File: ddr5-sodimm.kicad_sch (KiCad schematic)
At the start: 1 part, among them J4001 BUS_DDR5_SODIMM_AMPHENOL_1016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

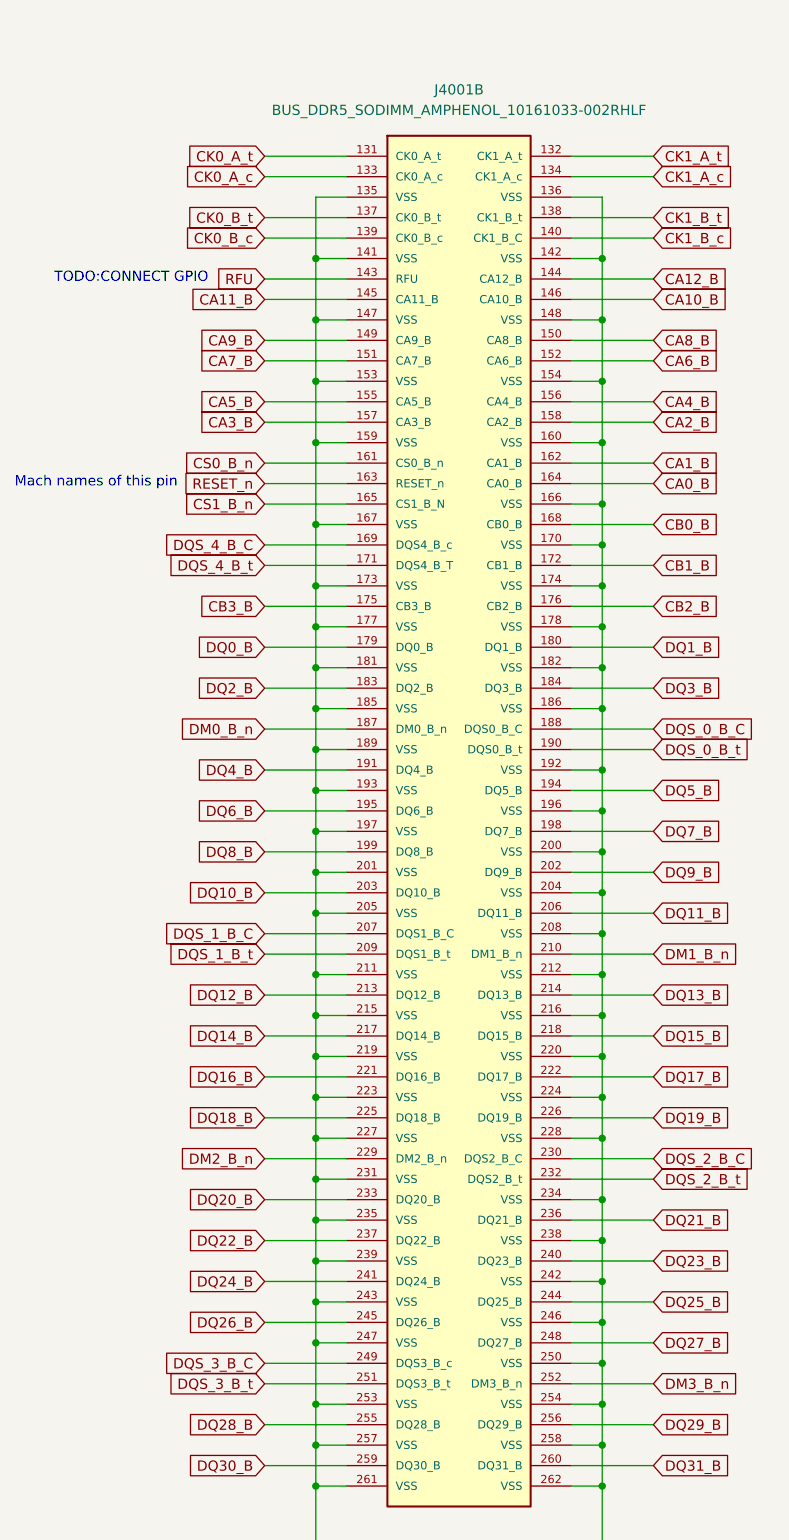
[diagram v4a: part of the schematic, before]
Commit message: Create pinout and fanout for FPGA bank 34
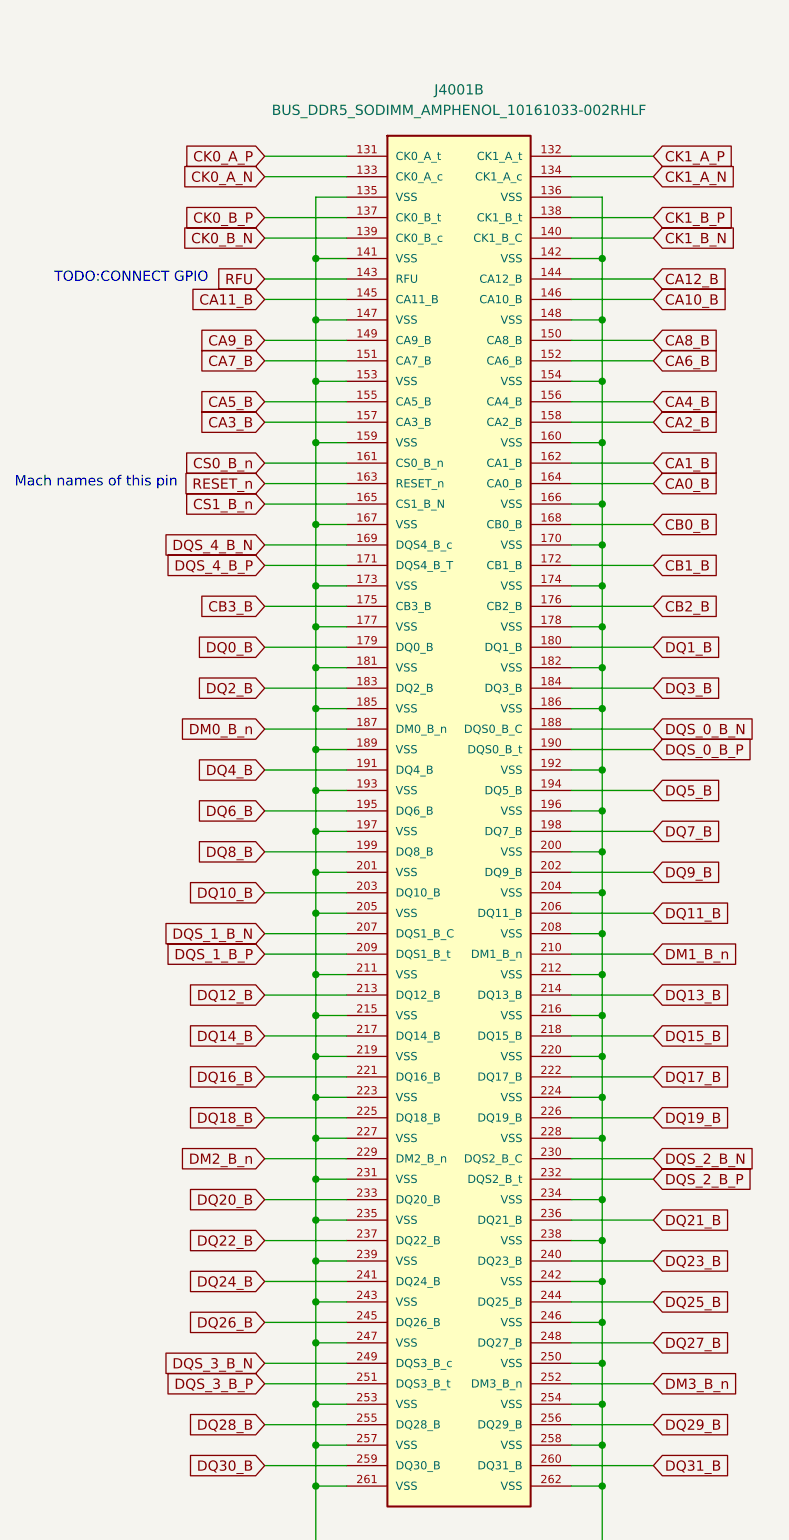
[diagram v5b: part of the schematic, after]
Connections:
- net CK0_A_c renamed CK0_A_N
- net CK0_A_t renamed CK0_A_P
- net CK0_B_c renamed CK0_B_N
- net CK0_B_t renamed CK0_B_P
- net CK1_A_c renamed CK1_A_N
- net CK1_A_t renamed CK1_A_P
- net CK1_B_c renamed CK1_B_N
- net CK1_B_t renamed CK1_B_P
- net DQS_0_B_C renamed DQS_0_B_N
- net DQS_0_B_t renamed DQS_0_B_P
- net DQS_1_B_C renamed DQS_1_B_N
- net DQS_1_B_t renamed DQS_1_B_P
- net DQS_2_B_C renamed DQS_2_B_N
- net DQS_2_B_t renamed DQS_2_B_P
- net DQS_3_B_C renamed DQS_3_B_N
- net DQS_3_B_t renamed DQS_3_B_P
- net DQS_4_B_C renamed DQS_4_B_N
- net DQS_4_B_t renamed DQS_4_B_P
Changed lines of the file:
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@@
     )
   )
-  (global_label "CK1_B_c" (shape input) (at 318.77 61.595 0) (fields_autoplaced)
-    (effects (font (size 1.27 1.27)) (justify left))
-    (property "Intersheet References" "${INTERSHEET_REFS}" (id 0) (at 329.1375 61.5156 0)
+  (global_label "CK1_B_N" (shape input) (at 318.77 61.595 0) (fields_autoplaced)
+    (effects (font (size 1.27 1.27)) (justify left))
+    (property "Intersheet References" "${INTERSHEET_REFS}" (id 0) (at 329.3794 61.5156 0)
       (effects (font (size 1.27 1.27)) (justify left) hide)
     )
@@
     )
   )
-  (global_label "DQS_4_B_t" (shape input) (at 270.51 102.235 180) (fields_autoplaced)
-    (effects (font (size 1.27 1.27)) (justify right))
-    (property "Intersheet References" "${INTERSHEET_REFS}" (id 0) (at 258.2677 102.1556 0)
+  (global_label "DQS_4_B_P" (shape input) (at 270.51 102.235 180) (fields_autoplaced)
+    (effects (font (size 1.27 1.27)) (justify right))
+    (property "Intersheet References" "${INTERSHEET_REFS}" (id 0) (at 257.7234 102.1556 0)
       (effects (font (size 1.27 1.27)) (justify right) hide)
     )
@@
     )
   )
-  (global_label "CK0_A_t" (shape input) (at 270.51 51.435 180) (fields_autoplaced)
-    (effects (font (size 1.27 1.27)) (justify right))
-    (property "Intersheet References" "${INTERSHEET_REFS}" (id 0) (at 260.6868 51.3556 0)
+  (global_label "CK0_A_P" (shape input) (at 270.51 51.435 180) (fields_autoplaced)
+    (effects (font (size 1.27 1.27)) (justify right))
+    (property "Intersheet References" "${INTERSHEET_REFS}" (id 0) (at 260.1425 51.3556 0)
       (effects (font (size 1.27 1.27)) (justify right) hide)
     )
@@
     )
   )
-  (global_label "DQS_0_B_t" (shape input) (at 318.77 125.095 0) (fields_autoplaced)
-    (effects (font (size 1.27 1.27)) (justify left))
-    (property "Intersheet References" "${INTERSHEET_REFS}" (id 0) (at 331.0123 125.0156 0)
+  (global_label "DQS_0_B_P" (shape input) (at 318.77 125.095 0) (fields_autoplaced)
+    (effects (font (size 1.27 1.27)) (justify left))
+    (property "Intersheet References" "${INTERSHEET_REFS}" (id 0) (at 331.5566 125.0156 0)
       (effects (font (size 1.27 1.27)) (justify left) hide)
     )
@@
     )
   )
-  (global_label "CK1_B_t" (shape input) (at 318.77 59.055 0) (fields_autoplaced)
-    (effects (font (size 1.27 1.27)) (justify left))
-    (property "Intersheet References" "${INTERSHEET_REFS}" (id 0) (at 328.7747 58.9756 0)
+  (global_label "CK1_B_P" (shape input) (at 318.77 59.055 0) (fields_autoplaced)
+    (effects (font (size 1.27 1.27)) (justify left))
+    (property "Intersheet References" "${INTERSHEET_REFS}" (id 0) (at 329.319 58.9756 0)
       (effects (font (size 1.27 1.27)) (justify left) hide)
     )
@@
     )
   )
-  (global_label "DQS_2_B_C" (shape input) (at 318.77 175.895 0) (fields_autoplaced)
-    (effects (font (size 1.27 1.27)) (justify left))
-    (property "Intersheet References" "${INTERSHEET_REFS}" (id 0) (at 331.5566 175.8156 0)
+  (global_label "DQS_2_B_N" (shape input) (at 318.77 175.895 0) (fields_autoplaced)
+    (effects (font (size 1.27 1.27)) (justify left))
+    (property "Intersheet References" "${INTERSHEET_REFS}" (id 0) (at 331.6171 175.8156 0)
       (effects (font (size 1.27 1.27)) (justify left) hide)
     )
@@
     )
   )
-  (global_label "DQS_3_B_t" (shape input) (at 270.51 203.835 180) (fields_autoplaced)
-    (effects (font (size 1.27 1.27)) (justify right))
-    (property "Intersheet References" "${INTERSHEET_REFS}" (id 0) (at 258.2677 203.7556 0)
+  (global_label "DQS_3_B_P" (shape input) (at 270.51 203.835 180) (fields_autoplaced)
+    (effects (font (size 1.27 1.27)) (justify right))
+    (property "Intersheet References" "${INTERSHEET_REFS}" (id 0) (at 257.7234 203.7556 0)
       (effects (font (size 1.27 1.27)) (justify right) hide)
     )
@@
     )
   )
-  (global_label "DQS_3_B_C" (shape input) (at 270.51 201.295 180) (fields_autoplaced)
-    (effects (font (size 1.27 1.27)) (justify right))
-    (property "Intersheet References" "${INTERSHEET_REFS}" (id 0) (at 257.7234 201.2156 0)
+  (global_label "DQS_3_B_N" (shape input) (at 270.51 201.295 180) (fields_autoplaced)
+    (effects (font (size 1.27 1.27)) (justify right))
+    (property "Intersheet References" "${INTERSHEET_REFS}" (id 0) (at 257.6629 201.2156 0)
       (effects (font (size 1.27 1.27)) (justify right) hide)
     )
@@
     )
   )
-  (global_label "DQS_1_B_C" (shape input) (at 270.51 147.955 180) (fields_autoplaced)
-    (effects (font (size 1.27 1.27)) (justify right))
-    (property "Intersheet References" "${INTERSHEET_REFS}" (id 0) (at 257.7234 147.8756 0)
+  (global_label "DQS_1_B_N" (shape input) (at 270.51 147.955 180) (fields_autoplaced)
+    (effects (font (size 1.27 1.27)) (justify right))
+    (property "Intersheet References" "${INTERSHEET_REFS}" (id 0) (at 257.6629 147.8756 0)
       (effects (font (size 1.27 1.27)) (justify right) hide)
     )
@@
     )
   )
-  (global_label "CK0_B_t" (shape input) (at 270.51 59.055 180) (fields_autoplaced)
-    (effects (font (size 1.27 1.27)) (justify right))
-    (property "Intersheet References" "${INTERSHEET_REFS}" (id 0) (at 260.5053 58.9756 0)
+  (global_label "CK0_B_P" (shape input) (at 270.51 59.055 180) (fields_autoplaced)
+    (effects (font (size 1.27 1.27)) (justify right))
+    (property "Intersheet References" "${INTERSHEET_REFS}" (id 0) (at 259.961 58.9756 0)
       (effects (font (size 1.27 1.27)) (justify right) hide)
     )
@@
     )
   )
-  (global_label "CK0_B_c" (shape input) (at 270.51 61.595 180) (fields_autoplaced)
-    (effects (font (size 1.27 1.27)) (justify right))
-    (property "Intersheet References" "${INTERSHEET_REFS}" (id 0) (at 260.1425 61.5156 0)
+  (global_label "CK0_B_N" (shape input) (at 270.51 61.595 180) (fields_autoplaced)
+    (effects (font (size 1.27 1.27)) (justify right))
+    (property "Intersheet References" "${INTERSHEET_REFS}" (id 0) (at 259.9006 61.5156 0)
       (effects (font (size 1.27 1.27)) (justify right) hide)
     )
@@
     )
   )
-  (global_label "CK1_A_c" (shape input) (at 318.77 53.975 0) (fields_autoplaced)
-    (effects (font (size 1.27 1.27)) (justify left))
-    (property "Intersheet References" "${INTERSHEET_REFS}" (id 0) (at 328.9561 53.8956 0)
+  (global_label "CK1_A_N" (shape input) (at 318.77 53.975 0) (fields_autoplaced)
+    (effects (font (size 1.27 1.27)) (justify left))
+    (property "Intersheet References" "${INTERSHEET_REFS}" (id 0) (at 329.198 53.8956 0)
       (effects (font (size 1.27 1.27)) (justify left) hide)
     )
@@
     )
   )
-  (global_label "DQS_4_B_C" (shape input) (at 270.51 99.695 180) (fields_autoplaced)
-    (effects (font (size 1.27 1.27)) (justify right))
-    (property "Intersheet References" "${INTERSHEET_REFS}" (id 0) (at 257.7234 99.6156 0)
+  (global_label "DQS_4_B_N" (shape input) (at 270.51 99.695 180) (fields_autoplaced)
+    (effects (font (size 1.27 1.27)) (justify right))
+    (property "Intersheet References" "${INTERSHEET_REFS}" (id 0) (at 257.6629 99.6156 0)
       (effects (font (size 1.27 1.27)) (justify right) hide)
     )
@@
     )
   )
-  (global_label "DQS_0_B_C" (shape input) (at 318.77 122.555 0) (fields_autoplaced)
-    (effects (font (size 1.27 1.27)) (justify left))
-    (property "Intersheet References" "${INTERSHEET_REFS}" (id 0) (at 331.5566 122.4756 0)
+  (global_label "DQS_0_B_N" (shape input) (at 318.77 122.555 0) (fields_autoplaced)
+    (effects (font (size 1.27 1.27)) (justify left))
+    (property "Intersheet References" "${INTERSHEET_REFS}" (id 0) (at 331.6171 122.4756 0)
       (effects (font (size 1.27 1.27)) (justify left) hide)
     )
@@
     )
   )
-  (global_label "CK0_A_c" (shape input) (at 270.51 53.975 180) (fields_autoplaced)
-    (effects (font (size 1.27 1.27)) (justify right))
-    (property "Intersheet References" "${INTERSHEET_REFS}" (id 0) (at 260.3239 53.8956 0)
+  (global_label "CK0_A_N" (shape input) (at 270.51 53.975 180) (fields_autoplaced)
+    (effects (font (size 1.27 1.27)) (justify right))
+    (property "Intersheet References" "${INTERSHEET_REFS}" (id 0) (at 260.082 53.8956 0)
       (effects (font (size 1.27 1.27)) (justify right) hide)
     )
@@
     )
   )
-  (global_label "DQS_2_B_t" (shape input) (at 318.77 178.435 0) (fields_autoplaced)
-    (effects (font (size 1.27 1.27)) (justify left))
-    (property "Intersheet References" "${INTERSHEET_REFS}" (id 0) (at 331.0123 178.3556 0)
-      (effects (font (size 1.27 1.27)) (justify left) hide)
-    )
-  )
-  (global_label "CK1_A_t" (shape input) (at 318.77 51.435 0) (fields_autoplaced)
-    (effects (font (size 1.27 1.27)) (justify left))
-    (property "Intersheet References" "${INTERSHEET_REFS}" (id 0) (at 328.5932 51.3556 0)
+  (global_label "DQS_2_B_P" (shape input) (at 318.77 178.435 0) (fields_autoplaced)
+    (effects (font (size 1.27 1.27)) (justify left))
+    (property "Intersheet References" "${INTERSHEET_REFS}" (id 0) (at 331.5566 178.3556 0)
+      (effects (font (size 1.27 1.27)) (justify left) hide)
+    )
+  )
+  (global_label "CK1_A_P" (shape input) (at 318.77 51.435 0) (fields_autoplaced)
+    (effects (font (size 1.27 1.27)) (justify left))
+    (property "Intersheet References" "${INTERSHEET_REFS}" (id 0) (at 329.1375 51.3556 0)
       (effects (font (size 1.27 1.27)) (justify left) hide)
     )
@@
     )
   )
-  (global_label "DQS_1_B_t" (shape input) (at 270.51 150.495 180) (fields_autoplaced)
-    (effects (font (size 1.27 1.27)) (justify right))
-    (property "Intersheet References" "${INTERSHEET_REFS}" (id 0) (at 258.2677 150.4156 0)
-      (effects (font (size 1.27 1.27)) (justify right) hide)
-    )
+  (global_label "DQS_1_B_P" (shape input) (at 270.51 150.495 180) (fields_autoplaced)
+    (effects (font (size 1.27 1.27)) (justify right))
+    (property "Intersheet References" "${INTERSHEET_REFS}" (id 0) (at 257.7234 150.4156 0)
+      (effects (font (size 1.27 1.27)) (justify right) hide)
+    )

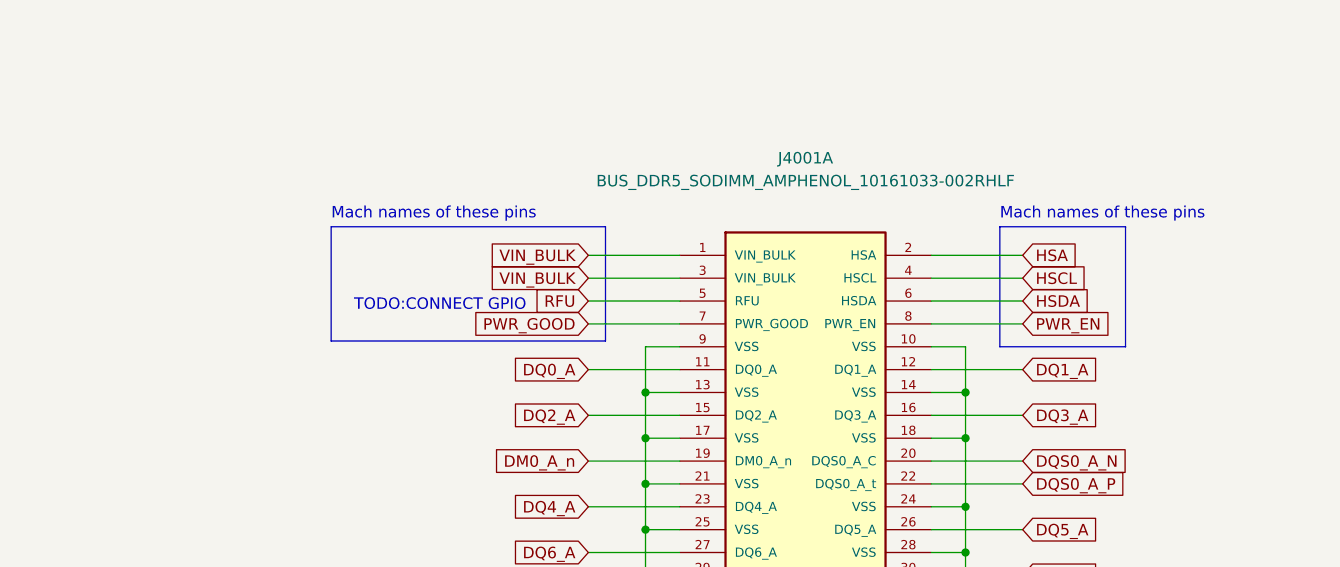
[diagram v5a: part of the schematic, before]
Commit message: Replace supply labels with proper symbols
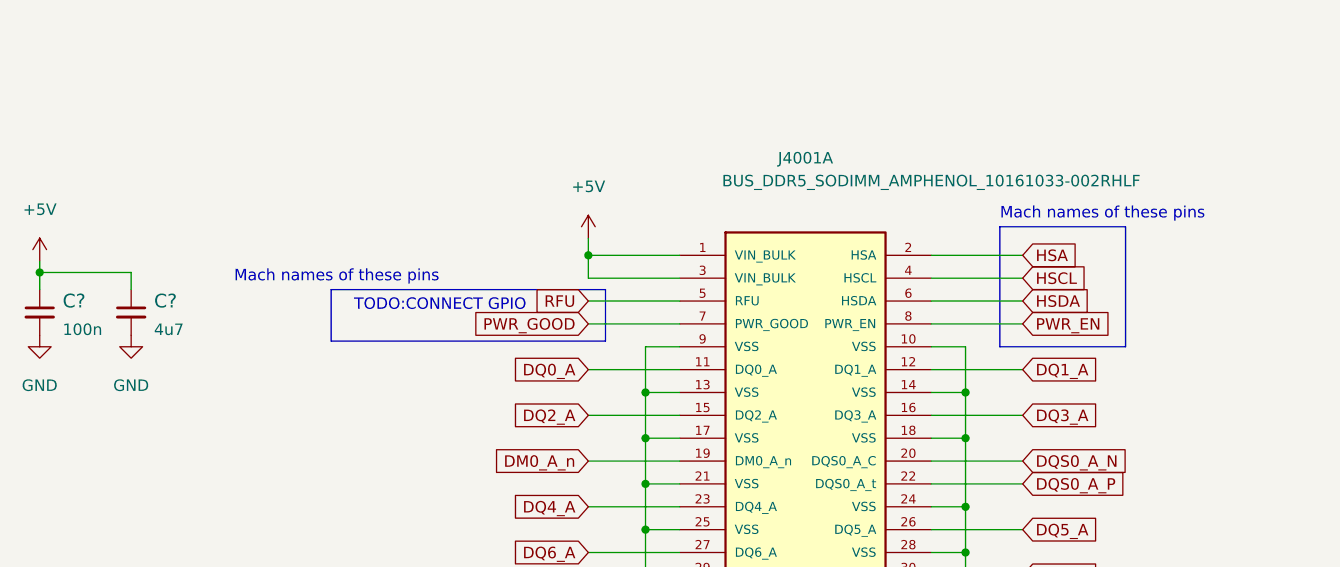
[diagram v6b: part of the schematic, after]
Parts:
- added C?: C_100n_0201, data-center-rdimm-ddr4-tester-footprints:C_0201, symbol data-center-rdimm-ddr4-tester:C_100n_0201
- added C?: C_4u7_0402, data-center-rdimm-ddr4-tester-footprints:C_0402_1005Metric, symbol data-center-rdimm-ddr4-tester:C_4u7_0402
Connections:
- net GND: now also C?.2, C?.2
- net VIN_BULK renamed +5V
- net +5V: now also C?.1, C?.1

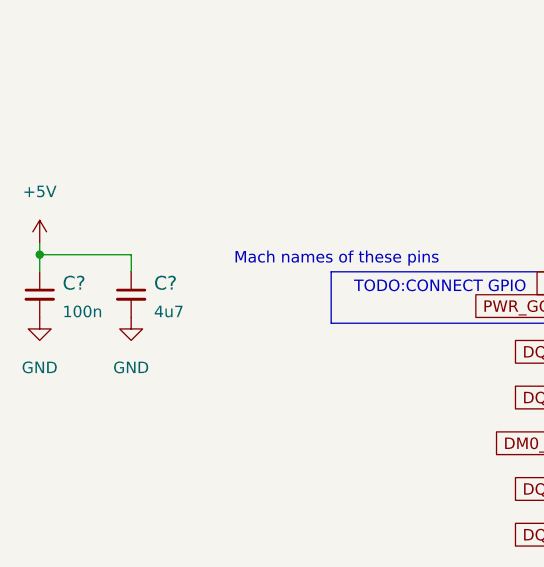
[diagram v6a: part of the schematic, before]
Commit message: Create FPGA decoupling, start creating power planes
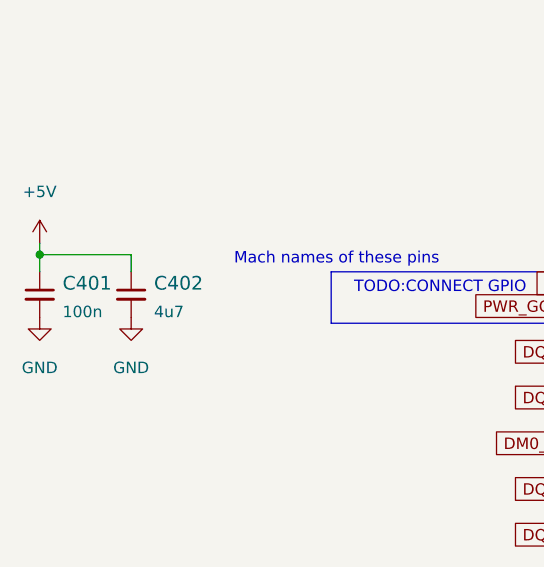
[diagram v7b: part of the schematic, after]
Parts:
- gave numbers to parts that had none: 2
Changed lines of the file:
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@@
   (symbol (lib_id "power:+5V") (at 28.575 52.07 0) (unit 1)
     (in_bom yes) (on_board yes) (fields_autoplaced)
-    (property "Reference" "#PWR?" (id 0) (at 28.575 55.88 0)
+    (property "Reference" "#PWR0129" (id 0) (at 28.575 55.88 0)
       (effects (font (size 1.27 1.27)) hide)
     )
@@
   (symbol (lib_id "power:+5V") (at 89.535 49.53 0) (unit 1)
     (in_bom yes) (on_board yes) (fields_autoplaced)
-    (property "Reference" "#PWR?" (id 0) (at 89.535 53.34 0)
+    (property "Reference" "#PWR0128" (id 0) (at 89.535 53.34 0)
       (effects (font (size 1.27 1.27)) hide)
     )
@@
   (symbol (lib_id "data-center-rdimm-ddr4-tester:C_100n_0201") (at 28.575 55.245 270) (unit 1)
     (in_bom yes) (on_board yes) (fields_autoplaced)
-    (property "Reference" "C?" (id 0) (at 31.115 56.5213 90)
+    (property "Reference" "C401" (id 0) (at 31.115 56.5213 90)
       (effects (font (size 1.524 1.524)) (justify left))
     )
@@
   (symbol (lib_id "data-center-rdimm-ddr4-tester:C_4u7_0402") (at 38.735 55.245 270) (unit 1)
     (in_bom yes) (on_board yes) (fields_autoplaced)
-    (property "Reference" "C?" (id 0) (at 41.275 56.5213 90)
+    (property "Reference" "C402" (id 0) (at 41.275 56.5213 90)
       (effects (font (size 1.524 1.524)) (justify left))
     )
@@
   (symbol (lib_id "data-center-rdimm-ddr4-tester:GND") (at 38.735 60.325 0) (unit 1)
     (in_bom yes) (on_board yes) (fields_autoplaced)
-    (property "Reference" "#PWR?" (id 0) (at 38.735 66.675 0)
+    (property "Reference" "#PWR0126" (id 0) (at 38.735 66.675 0)
       (effects (font (size 1.27 1.27)) hide)
     )
@@
   (symbol (lib_id "data-center-rdimm-ddr4-tester:GND") (at 28.575 60.325 0) (unit 1)
     (in_bom yes) (on_board yes) (fields_autoplaced)
-    (property "Reference" "#PWR?" (id 0) (at 28.575 66.675 0)
-      (effects (font (size 1.27 1.27)) hide)
-    )
+    (property "Reference" "#PWR0127" (id 0) (at 28.575 66.675 0)
+      (effects (font (size 1.27 1.27)) hide)
+    )
